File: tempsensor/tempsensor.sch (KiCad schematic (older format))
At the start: 16 parts, among them J1 Conn_01x14, SW1 SW_DIP_x06, SW2 PW_ON, U1 MKW41Z512VHT, Y1 32MHz 10PPM SMT 2.0x1.6mm 10PF, Y2 32.768KHz 20PPM 3.2x1.5mm 7PF

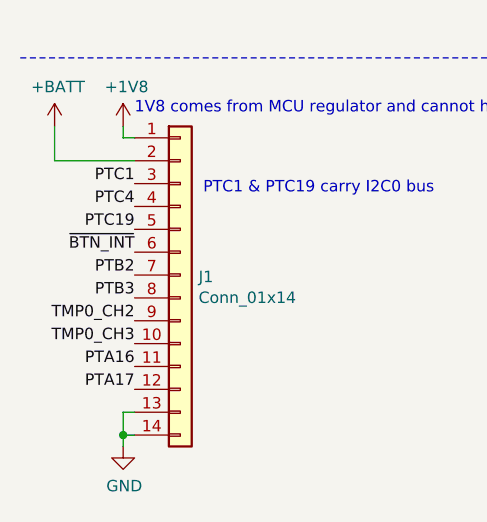
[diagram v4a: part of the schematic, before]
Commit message: Started layouting the TempSensor, exchanged the large LEDs for 0603 LEDs (from ELAB). MCU needs to be placed. Changed signals on expansion header to put power pins onto just one end.
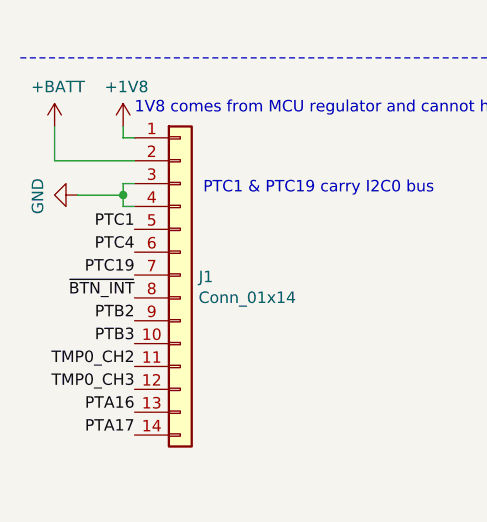
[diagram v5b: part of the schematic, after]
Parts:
- AE1: footprint RF_Antenna:Texas_SWRA117D_2.4GHz_Left -> RF_Antenna:Texas_SWRA117D_2.4GHz_Right
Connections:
- net GND: now also J1.3 (Pin_3), J1.4 (Pin_4); no longer J1.13 (Pin_13), J1.14 (Pin_14)
- net PTA16: now also J1.13 (Pin_13); no longer J1.11 (Pin_11)
- net PTA17: now also J1.14 (Pin_14); no longer J1.12 (Pin_12)
- net PTB2: now also J1.9 (Pin_9); no longer J1.7 (Pin_7)
- net PTB3: now also J1.10 (Pin_10); no longer J1.8 (Pin_8)
- net PTC1: now also J1.5 (Pin_5); no longer J1.3 (Pin_3)
- net PTC19: now also J1.7 (Pin_7); no longer J1.5 (Pin_5)
- net PTC4: now also J1.6 (Pin_6); no longer J1.4 (Pin_4)
- net TMP0_CH2: now also J1.11 (Pin_11); no longer J1.9 (Pin_9)
- net TMP0_CH3: now also J1.12 (Pin_12); no longer J1.10 (Pin_10)
- net ~BTN_INT: now also J1.8 (Pin_8); no longer J1.6 (Pin_6)
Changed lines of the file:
@@
 Wire Wire Line
 	7050 3350 6600 3350
-Text Label 1000 6950 2    50   ~ 0
+Text Label 1000 7150 2    50   ~ 0
 TMP0_CH2
 Text Label 7050 2650 2    50   ~ 0
@@
 Wire Wire Line
 	7050 4650 6600 4650
+Text Label 1000 7250 2    50   ~ 0
+TMP0_CH3
+Text Label 1000 6950 2    50   ~ 0
+PTB2
 Text Label 1000 7050 2    50   ~ 0
-TMP0_CH3
-Text Label 1000 6750 2    50   ~ 0
-PTB2
+PTB3
+Text Label 1000 7350 2    50   ~ 0
+PTA16
 Text Label 1000 6850 2    50   ~ 0
-PTB3
-Text Label 1000 7150 2    50   ~ 0
-PTA16
-Text Label 1000 6650 2    50   ~ 0
 ~BTN_INT
 Text Label 6950 4550 2    50   ~ 0
 PTA17
-Text Label 1000 7250 2    50   ~ 0
+Text Label 1000 7450 2    50   ~ 0
 PTA17
 Text Notes 7000 3600 0    50   ~ 0
@@
 L power:GND #PWR016
 U 1 1 5FA3DB1B
-P 950 7500
-F 0 "#PWR016" H 950 7250 50  0001 C CNN
-F 1 "GND" H 955 7327 50  0000 C CNN
-F 2 "" H 950 7500 50  0001 C CNN
-F 3 "" H 950 7500 50  0001 C CNN
-	1    950  7500
-	1    0    0    -1
-$EndComp
-Wire Wire Line
-	1000 7350 950  7350
-Wire Wire Line
-	950  7350 950  7450
-Wire Wire Line
-	1000 7450 950  7450
-Connection ~ 950  7450
-Wire Wire Line
-	950  7450 950  7500
+P 750 6400
+F 0 "#PWR016" H 750 6150 50  0001 C CNN
+F 1 "GND" H 755 6227 50  0000 C CNN
+F 2 "" H 750 6400 50  0001 C CNN
+F 3 "" H 750 6400 50  0001 C CNN
+	1    750  6400
+	0    1    1    0
+$EndComp
 $Comp
 L Device:Antenna_Shield AE1
@@
 F 0 "AE1" V 8686 5280 50  0000 L CNN
 F 1 "Antenna_Shield" V 8777 5280 50  0000 L CNN
-F 2 "RF_Antenna:Texas_SWRA117D_2.4GHz_Left" H 8700 5150 50  0001 C CNN
+F 2 "RF_Antenna:Texas_SWRA117D_2.4GHz_Right" H 8700 5150 50  0001 C CNN
 F 3 "~" H 8700 5150 50  0001 C CNN
 	1    8700 5050
@@
 Wire Wire Line
 	12100 3000 12600 3000
-Text Label 1000 6550 2    50   ~ 0
+Text Label 1000 6750 2    50   ~ 0
 PTC19
-Text Label 1000 6450 2    50   ~ 0
+Text Label 1000 6650 2    50   ~ 0
 PTC4
 $Comp
@@
 	1    0    0    -1
 $EndComp
-Text Label 1000 6350 2    50   ~ 0
+Text Label 1000 6550 2    50   ~ 0
 PTC1
 $Comp
@@
 	1    0    0    -1
 $EndComp
+Wire Wire Line
+	1000 6350 950  6350
+Wire Wire Line
+	950  6350 950  6400
+Wire Wire Line
+	950  6450 1000 6450
+Wire Wire Line
+	950  6400 750  6400
+Connection ~ 950  6400
+Wire Wire Line
+	950  6400 950  6450
 $EndSCHEMATC

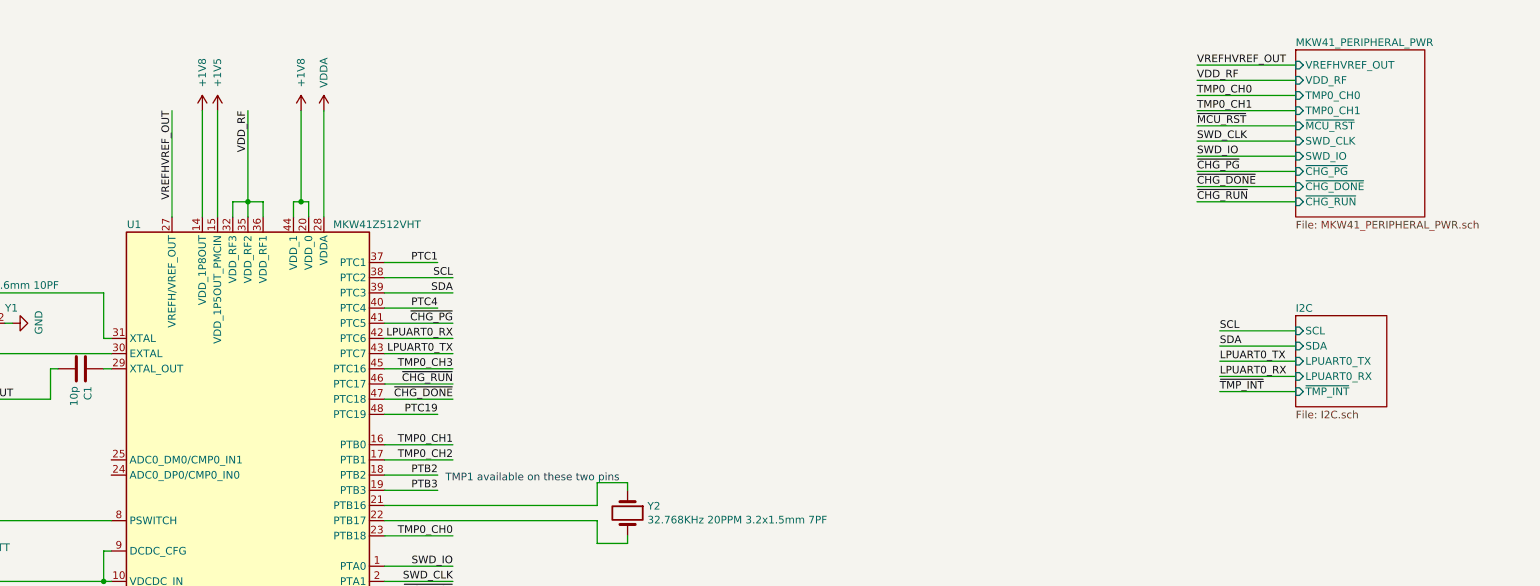
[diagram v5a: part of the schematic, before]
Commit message: Continued routing of tempsensor, basic functionality done.
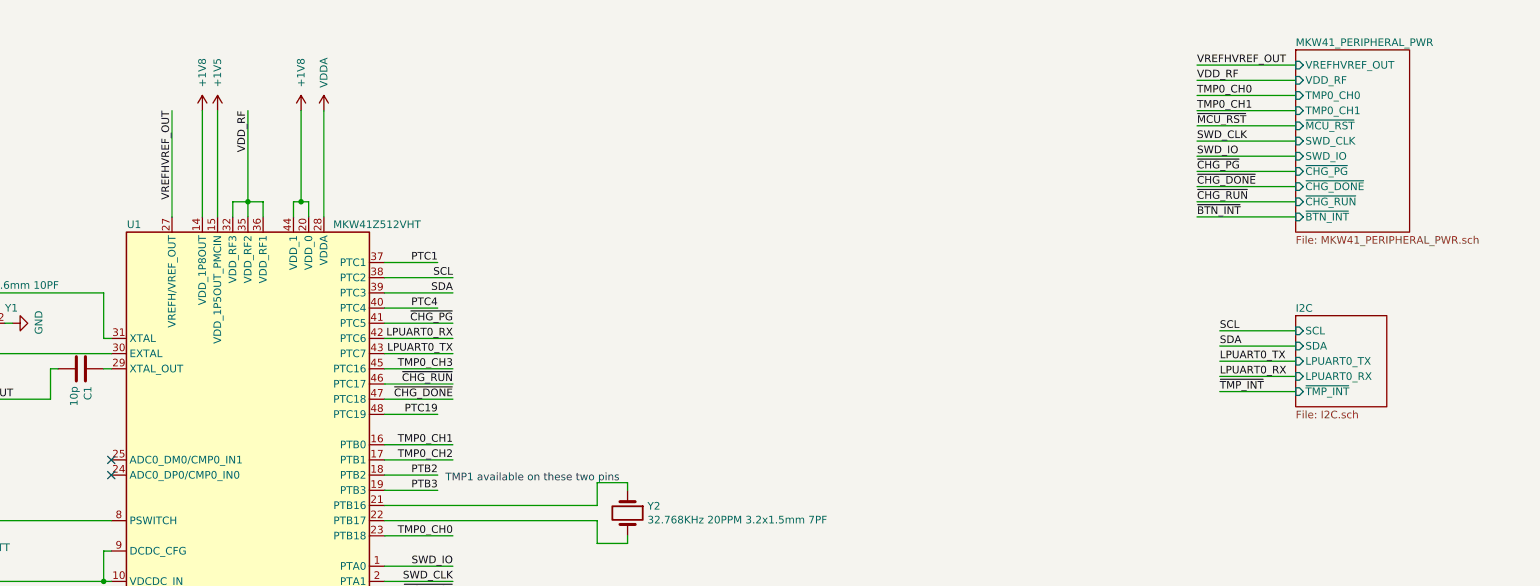
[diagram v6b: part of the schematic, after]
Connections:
- no-connect marks 0 -> 2
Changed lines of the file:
@@
 $EndSheet
 $Sheet
-S 12600 750  850  1100
+S 12600 750  750  1200
 U 5FB5B55F
 F0 "MKW41_PERIPHERAL_PWR" 50
@@
 F10 "~CHG_DONE" I L 12600 1650 50
 F11 "~CHG_RUN" I L 12600 1750 50
+F12 "~BTN_INT" I L 12600 1850 50
 $EndSheet
 Wire Notes Line
@@
 Wire Wire Line
 	950  6400 950  6450
+NoConn ~ 4800 3450
+NoConn ~ 4800 3550
+Text Label 11950 1850 0    50   ~ 0
+~BTN_INT
+Wire Wire Line
+	11950 1850 12600 1850
 $EndSCHEMATC

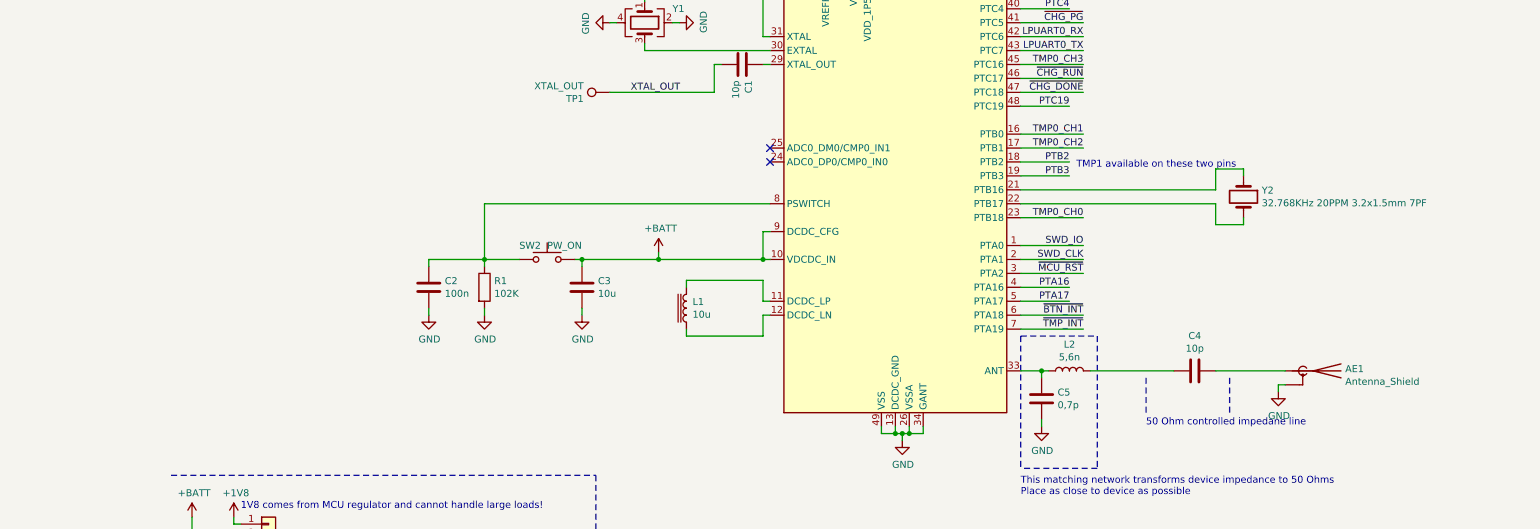
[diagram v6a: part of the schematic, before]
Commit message: Finished layouting tempsensor and thermostat. Parts are ordered from Mouser, PCB ordered from beta-layout.
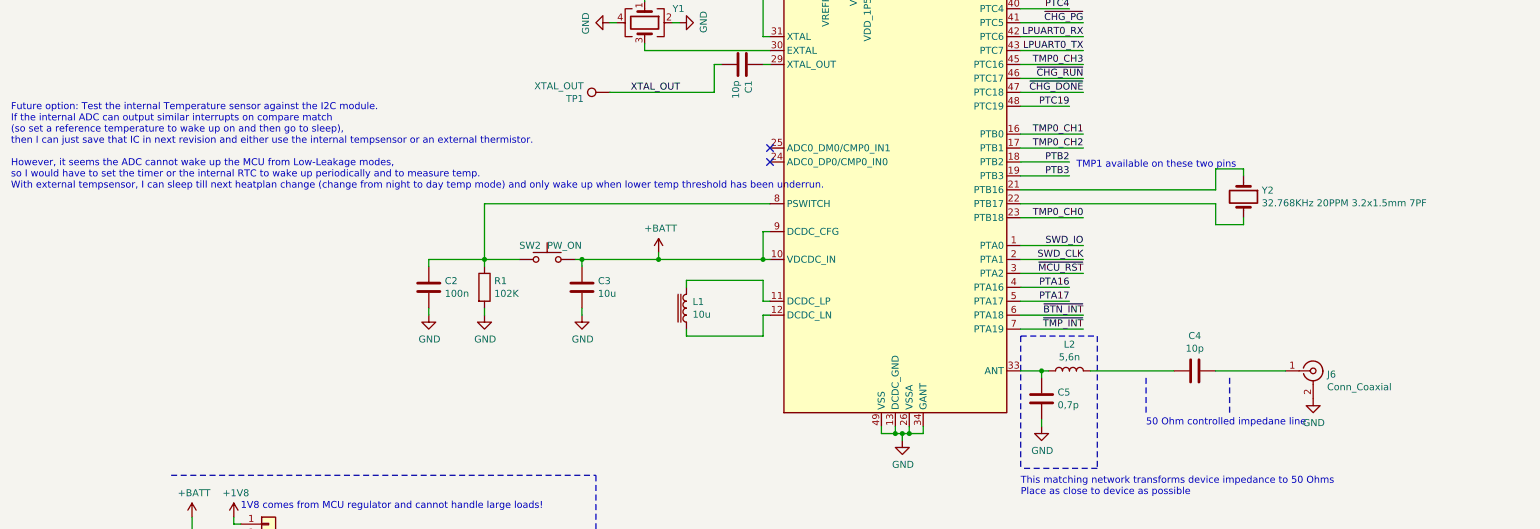
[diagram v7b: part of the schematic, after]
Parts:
- removed AE1: Antenna_Shield, RF_Antenna:Texas_SWRA117D_2.4GHz_Right, symbol Device:Antenna_Shield
- added J6: Conn_Coaxial, Connector_Coaxial:SMA_Amphenol_132289_EdgeMount, symbol Connector:Conn_Coaxial
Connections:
- net GND: now also J6.2 (Ext)
- net at C4.1: now also J6.1 (In)
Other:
- note added: "Future option: Test the internal Temperature sensor against the I2C module.\nIf the internal ADC can output similar interrupts on compare match \n(so set a reference temperature to wake up on and then go to sleep),\nthen I can just save that IC in next revision and either use the internal tempsensor or an external thermistor.\n\nHowever, it seems the ADC cannot wake up the MCU from Low-Leakage mo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"
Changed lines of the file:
@@
-	0    1    1    0
-$EndComp
-$Comp
-L Device:Antenna_Shield AE1
-U 1 1 5FEAE3EE
-P 8700 5050
-F 0 "AE1" V 8686 5280 50  0000 L CNN
-F 1 "Antenna_Shield" V 8777 5280 50  0000 L CNN
-F 2 "RF_Antenna:Texas_SWRA117D_2.4GHz_Right" H 8700 5150 50  0001 C CNN
-F 3 "~" H 8700 5150 50  0001 C CNN
-	1    8700 5050
 	0    1    1    0
 $EndComp
@@
 L power:GND #PWR011
 U 1 1 5FED4FC5
-P 8450 5200
-F 0 "#PWR011" H 8450 4950 50  0001 C CNN
-F 1 "GND" H 8455 5027 50  0000 C CNN
-F 2 "" H 8450 5200 50  0001 C CNN
-F 3 "" H 8450 5200 50  0001 C CNN
-	1    8450 5200
+P 8700 5250
+F 0 "#PWR011" H 8700 5000 50  0001 C CNN
+F 1 "GND" H 8705 5077 50  0000 C CNN
+F 2 "" H 8700 5250 50  0001 C CNN
+F 3 "" H 8700 5250 50  0001 C CNN
+	1    8700 5250
 	1    0    0    -1
 $EndComp
-Wire Wire Line
-	8450 5200 8450 5150
-Wire Wire Line
-	8450 5150 8500 5150
 Wire Notes Line
 	8100 5100 8100 5350
@@
 Wire Wire Line
 	11950 1850 12600 1850
+$Comp
+L Connector:Conn_Coaxial J6
+U 1 1 5FC59DB4
+P 8700 5050
+F 0 "J6" H 8800 5025 50  0000 L CNN
+F 1 "Conn_Coaxial" H 8800 4934 50  0000 L CNN
+F 2 "Connector_Coaxial:SMA_Amphenol_132289_EdgeMount" H 8700 5050 50  0001 C CNN
+F 3 " ~" H 8700 5050 50  0001 C CNN
+	1    8700 5050
+	1    0    0    -1
+$EndComp
+Text Notes -650 3750 0    50   ~ 0
+Future option: Test the internal Temperature sensor against the I2C module.\nIf the internal ADC can output similar interrupts on compare match \n(so set a reference temperature to wake up on and then go to sleep),\nthen I can just save that IC in next revision and either use the internal tempsensor or an external thermistor.\n\nHowever, it seems the ADC cannot wake up the MCU from Low-Leakage modes,\nso I would have to set the timer or the internal RTC to wake up periodically and to measure temp.\nWith external tempsensor, I can sleep till next heatplan change (change from night to day temp mode) and only wake up when lower temp threshold has been underrun.
 $EndSCHEMATC
